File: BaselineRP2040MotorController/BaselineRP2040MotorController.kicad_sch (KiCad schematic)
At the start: 2 parts, among them J4 XT60 Power Connector, J5 Conn_02x08_Odd_Even

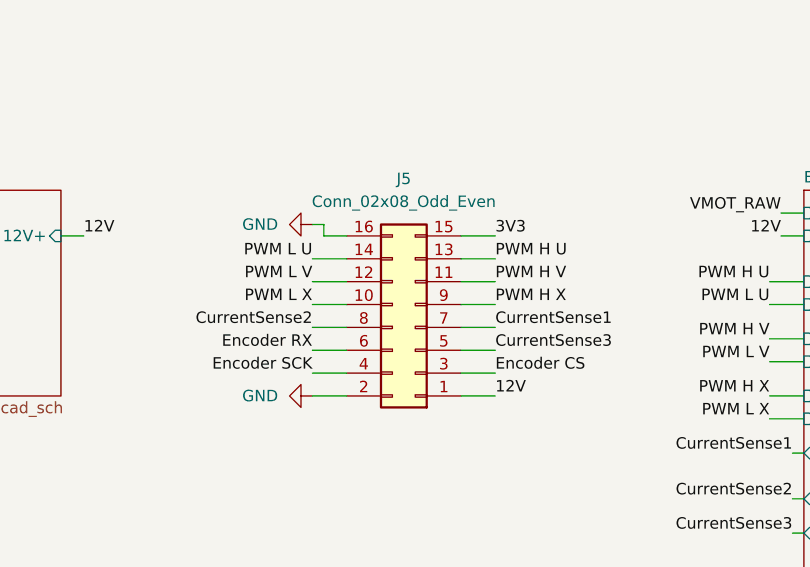
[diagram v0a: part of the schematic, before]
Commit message: Make a cut down board.
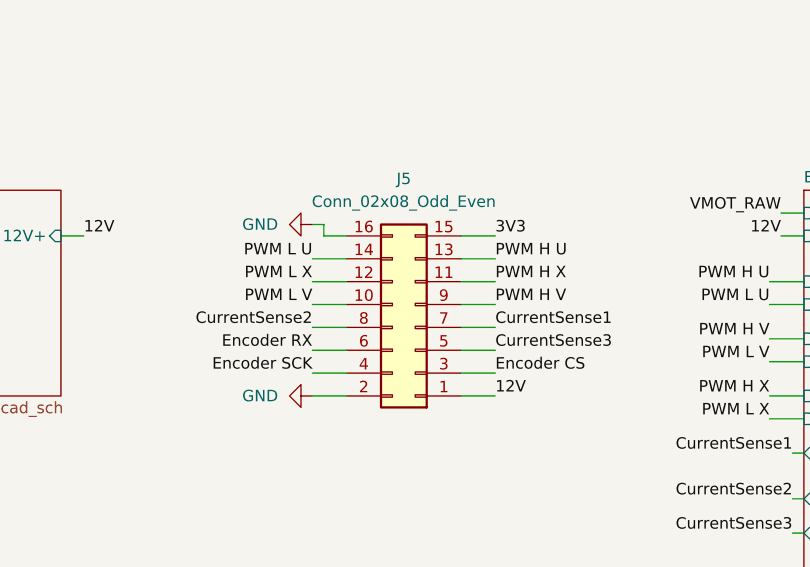
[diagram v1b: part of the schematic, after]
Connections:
- net PWM H V: now also J5.9 (Pin_9); no longer J5.11 (Pin_11)
- net PWM H X: now also J5.11 (Pin_11); no longer J5.9 (Pin_9)
- net PWM L V: now also J5.10 (Pin_10); no longer J5.12 (Pin_12)
- net PWM L X: now also J5.12 (Pin_12); no longer J5.10 (Pin_10)
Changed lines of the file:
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@@
-		)
-	)
-	(label "PWM L V"
-		(at 116.84 83.82 180)
-		(fields_autoplaced yes)
-		(effects
-			(font
-				(size 1.27 1.27)
-			)
-			(justify right bottom)
 		)
 	)
@@
 		)
 	)
-	(label "PWM H V"
-		(at 137.16 83.82 0)
-		(fields_autoplaced yes)
-		(effects
-			(font
-				(size 1.27 1.27)
-			)
-			(justify left bottom)
-		)
-	)
-	(label "PWM L X"
+	(label "PWM L V"
 		(at 116.84 86.36 180)
 		(fields_autoplaced yes)
@@
 		)
 	)
-	(label "PWM H X"
+	(label "PWM H V"
 		(at 137.16 86.36 0)
 		(fields_autoplaced yes)
@@
 		(fields_autoplaced yes)
 		(effects
+			(font
+				(size 1.27 1.27)
+			)
+			(justify right bottom)
+		)
+	)
+	(label "PWM H X"
+		(at 137.16 83.82 0)
+		(fields_autoplaced yes)
+		(effects
+			(font
+				(size 1.27 1.27)
+			)
+			(justify left bottom)
+		)
+	)
+	(label "PWM L X"
+		(at 116.84 83.82 180)
+		(fields_autoplaced yes)
+		(effects
